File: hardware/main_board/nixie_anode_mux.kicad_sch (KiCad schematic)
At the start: 39 parts, among them Q10 MMBTA42, Q11 MMBTA92, Q12 MMBTA42, Q13 MMBTA92, Q14 MMBTA42, Q15 MMBTA92, Q4 MMBTA92, Q5 MMBTA42, Q6 MMBTA42, Q7 MMBTA92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

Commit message: chore(hardware): update bom and LCSC SN
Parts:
- C41: LCSC PN (none) -> C106248
- C42: LCSC PN (none) -> C36911391
- Q10, Q12, Q14, Q5, Q6, Q8: LCSC PN (none) -> C916394
- Q11, Q13, Q15, Q4, Q7, Q9: LCSC PN (none) -> C20069146
- R21, R39, R43, R47, R51, R55: LCSC PN (none) -> C105578
- R34, R38, R42, R46, R50, R54: LCSC PN (none) -> C114622
- R35, R40, R44, R48, R52, R56: LCSC PN (none) -> C105579
- R36, R37, R41, R45, R49, R53: LCSC PN (none) -> C98220
- U13: LCSC PN (none) -> C546729

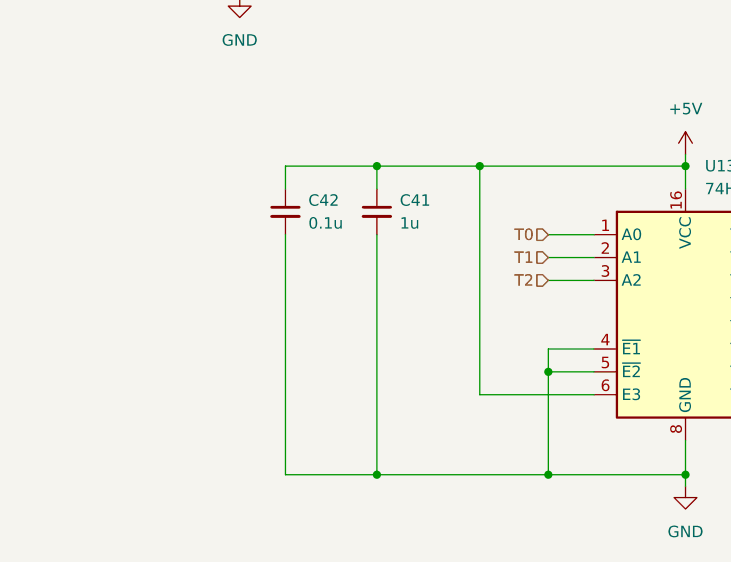
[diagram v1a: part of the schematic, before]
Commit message: hardware(schematic): update main control board schematic and layout
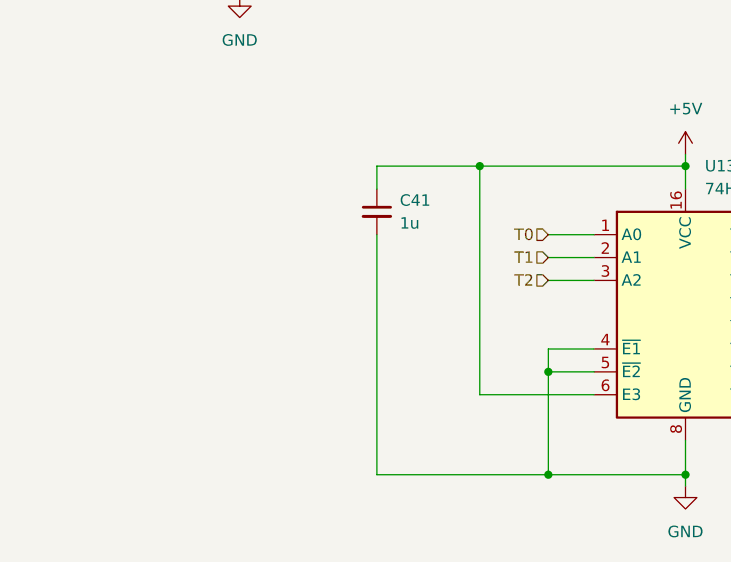
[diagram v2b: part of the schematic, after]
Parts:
- removed C42: 0.1u, Capacitor_SMD:C_0603_1608Metric, symbol Device:C_Small
- C41: LCSC PN C106248 -> C5199872
- Q10, Q12, Q14, Q5, Q6, Q8: LCSC PN C916394 -> C94389
- Q11, Q13, Q15, Q4, Q7, Q9: LCSC PN C20069146 -> C82049
- R21, R39, R43, R47, R51, R55: LCSC PN C105578 -> C22935
- R34, R38, R42, R46, R50, R54: LCSC PN C114622 -> C23178
- R35, R40, R44, R48, R52, R56: LCSC PN C105579 -> C25819
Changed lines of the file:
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@@
 	)
 	(junction
-		(at 55.88 176.53)
-		(diameter 0)
-		(color 0 0 0 0)
-	)
-	(junction
 		(at 125.73 49.53)
 		(diameter 0)
@@
 	)
 	(junction
-		(at 55.88 142.24)
-		(diameter 0)
-		(color 0 0 0 0)
-	)
-	(junction
 		(at 62.23 49.53)
 		(diameter 0)
@@
 	(wire
 		(pts
-			(xy 45.72 176.53) (xy 55.88 176.53)
-		)
-		(stroke
-			(width 0)
-			(type default)
-		)
-	)
-	(wire
-		(pts
 			(xy 190.5 30.48) (xy 190.5 36.83)
 		)
@@
 	(wire
 		(pts
-			(xy 45.72 144.78) (xy 45.72 142.24)
-		)
-		(stroke
-			(width 0)
-			(type default)
-		)
-	)
-	(wire
-		(pts
 			(xy 100.33 152.4) (xy 102.87 152.4)
 		)
@@
 	(wire
 		(pts
-			(xy 45.72 149.86) (xy 45.72 176.53)
-		)
-		(stroke
-			(width 0)
-			(type default)
-		)
-	)
-	(wire
-		(pts
 			(xy 30.48 113.03) (xy 33.02 113.03)
 		)
@@
 	(wire
 		(pts
-			(xy 45.72 142.24) (xy 55.88 142.24)
-		)
-		(stroke
-			(width 0)
-			(type default)
-		)
-	)
-	(wire
-		(pts
 			(xy 152.4 58.42) (xy 153.67 58.42)
 		)
@@
 			)
 		)
-		(property "LCSC PN" "C105578"
+		(property "LCSC PN" "C22935"
 			(at 180.34 45.72 0)
 			(effects
@@
 			)
 		)
-		(property "LCSC PN" "C114622"
+		(property "LCSC PN" "C23178"
 			(at 109.22 49.53 90)
 			(effects
@@
 			)
 		)
-		(property "LCSC PN" "C105579"
+		(property "LCSC PN" "C25819"
 			(at 201.93 106.68 90)
 			(effects
@@
 			)
 		)
-		(property "LCSC PN" "C106248"
+		(property "LCSC PN" "C5199872"
 			(at 55.88 147.32 0)
 			(effects
@@
 			)
 		)
-		(property "LCSC PN" "C105579"
+		(property "LCSC PN" "C25819"
 			(at 68.58 105.41 90)
 			(effects
@@
 			)
 		)
-		(property "LCSC PN" "C114622"
+		(property "LCSC PN" "C23178"
 			(at 45.72 105.41 90)
 			(effects
@@
 			)
 		)
-		(property "LCSC PN" "C916394"
+		(property "LCSC PN" "C94389"
 			(at 38.1 57.15 0)
 			(effects
@@
 			)
 		)
-		(property "LCSC PN" "C20069146"
+		(property "LCSC PN" "C82049"
 			(at 59.69 40.64 0)
 			(effects
@@
 			)
 		)
-		(property "LCSC PN" "C105579"
+		(property "LCSC PN" "C25819"
 			(at 196.85 50.8 90)
 			(effects
@@
 			)
 		)
-		(property "LCSC PN" "C105578"
+		(property "LCSC PN" "C22935"
 			(at 52.07 100.33 0)
 			(effects
@@
 			)
 		)
-		(property "LCSC PN" "C114622"
+		(property "LCSC PN" "C23178"
 			(at 110.49 105.41 90)
 			(effects
@@
 			)
 		)
-		(property "LCSC PN" "C20069146"
+		(property "LCSC PN" "C82049"
 			(at 59.69 96.52 0)
 			(effects
@@
 			)
 		)
-		(property "LCSC PN" "C105578"
+		(property "LCSC PN" "C22935"
 			(at 116.84 100.33 0)
 			(effects
@@
 			)
 		)
-		(property "LCSC PN" "C114622"
+		(property "LCSC PN" "C23178"
 			(at 45.72 49.53 90)
 			(effects
@@
 			)
 		)
-		(property "LCSC PN" "C105579"
+		(property "LCSC PN" "C25819"
 			(at 133.35 105.41 90)
 			(effects
@@
 			)
 		)
-		(property "LCSC PN" "C20069146"
+		(property "LCSC PN" "C82049"
 			(at 193.04 97.79 0)
 			(effects
@@
 			)
 		)
-		(property "LCSC PN" "C916394"
+		(property "LCSC PN" "C94389"
 			(at 171.45 114.3 0)
 			(effects
@@
 			)
 		)
-		(property "LCSC PN" "C114622"
+		(property "LCSC PN" "C23178"
 			(at 173.99 50.8 90)
 			(effects
@@
 			)
 		)
-		(property "LCSC PN" "C105578"
+		(property "LCSC PN" "C22935"
 			(at 185.42 101.6 0)
 			(effects
@@
 			)
 		)
-		(property "LCSC PN" "C20069146"
+		(property "LCSC PN" "C82049"
 			(at 187.96 41.91 0)
 			(effects
@@
 			)
 		)
-		(property "LCSC PN" "C916394"
+		(property "LCSC PN" "C94389"
 			(at 166.37 58.42 0)
 			(effects
@@
 			)
 		)
-		(property "LCSC PN" "C916394"
+		(property "LCSC PN" "C94389"
 			(at 38.1 113.03 0)
 			(effects
@@
 			)
 		)
-		(property "LCSC PN" "C916394"
+		(property "LCSC PN" "C94389"
 			(at 101.6 57.15 0)
 			(effects
@@
 			)
 		)
-		(property "LCSC PN" "C105579"
+		(property "LCSC PN" "C25819"
 			(at 132.08 49.53 90)
 			(effects
@@
 			)
 		)
-		(property "LCSC PN" "C105579"
+		(property "LCSC PN" "C25819"
 			(at 68.58 49.53 90)
 			(effects
@@
 			)
 		)
-		(property "LCSC PN" "C114622"
+		(property "LCSC PN" "C23178"
 			(at 179.07 106.68 90)
 			(effects
@@
 	)
 	(symbol
-		(lib_id "Device:C_Small")
-		(at 45.72 147.32 0)
-		(unit 1)
-		(exclude_from_sim no)
-		(in_bom yes)
-		(on_board yes)
-		(dnp no)
-		(fields_autoplaced yes)
-		(property "Reference" "C42"
-			(at 48.26 146.0562 0)
-			(effects
-				(font
-					(size 1.27 1.27)
-				)
-				(justify left)
-			)
-		)
-		(property "Value" "0.1u"
-			(at 48.26 148.5962 0)
-			(effects
-				(font
-					(size 1.27 1.27)
-				)
-				(justify left)
-			)
-		)
-		(property "Footprint" "Capacitor_SMD:C_0603_1608Metric"
-			(at 45.72 147.32 0)
-			(effects
-				(font
-					(size 1.27 1.27)
-				)
-				(hide yes)
-			)
-		)
-		(property "Datasheet" "~"
-			(at 45.72 147.32 0)
-			(effects
-				(font
-					(size 1.27 1.27)
-				)
-				(hide yes)
-			)
-		)
-		(property "Description" "Unpolarized capacitor, small symbol"
-			(at 45.72 147.32 0)
-			(effects
-				(font
-					(size 1.27 1.27)
-				)
-				(hide yes)
-			)
-		)
-		(property "LCSC PN" "C36911391"
-			(at 45.72 147.32 0)
-			(effects
-				(font
-					(size 1.27 1.27)
-				)
-				(hide yes)
-			)
-		)
-		(pin "1"
-		)
-		(pin "2"
-		)
-		(instances
-			(project "main_board"
-				(path "/62950e93-3f98-4dee-9256-8213caa98ee7/0cd333dd-e8ef-4279-9123-81fa88a25cdb"
-					(reference "C42")
-					(unit 1)
-				)
-			)
-		)
-	)
-	(symbol
 		(lib_id "Transistor_BJT:MMBTA92")
 		(at 123.19 40.64 0)
@@
 			)
 		)
-		(property "LCSC PN" "C20069146"
+		(property "LCSC PN" "C82049"
 			(at 123.19 40.64 0)
 			(effects
@@
 			)
 		)
-		(property "LCSC PN" "C20069146"
+		(property "LCSC PN" "C82049"
 			(at 124.46 96.52 0)
 			(effects
@@
 			)
 		)
-		(property "LCSC PN" "C916394"
+		(property "LCSC PN" "C94389"
 			(at 102.87 113.03 0)
 			(effects
@@
 			)
 		)
-		(property "LCSC PN" "C105578"
+		(property "LCSC PN" "C22935"
 			(at 52.07 44.45 0)
 			(effects
@@
 			)
 		)
-		(property "LCSC PN" "C105578"
+		(property "LCSC PN" "C22935"
 			(at 115.57 44.45 0)
 			(effects

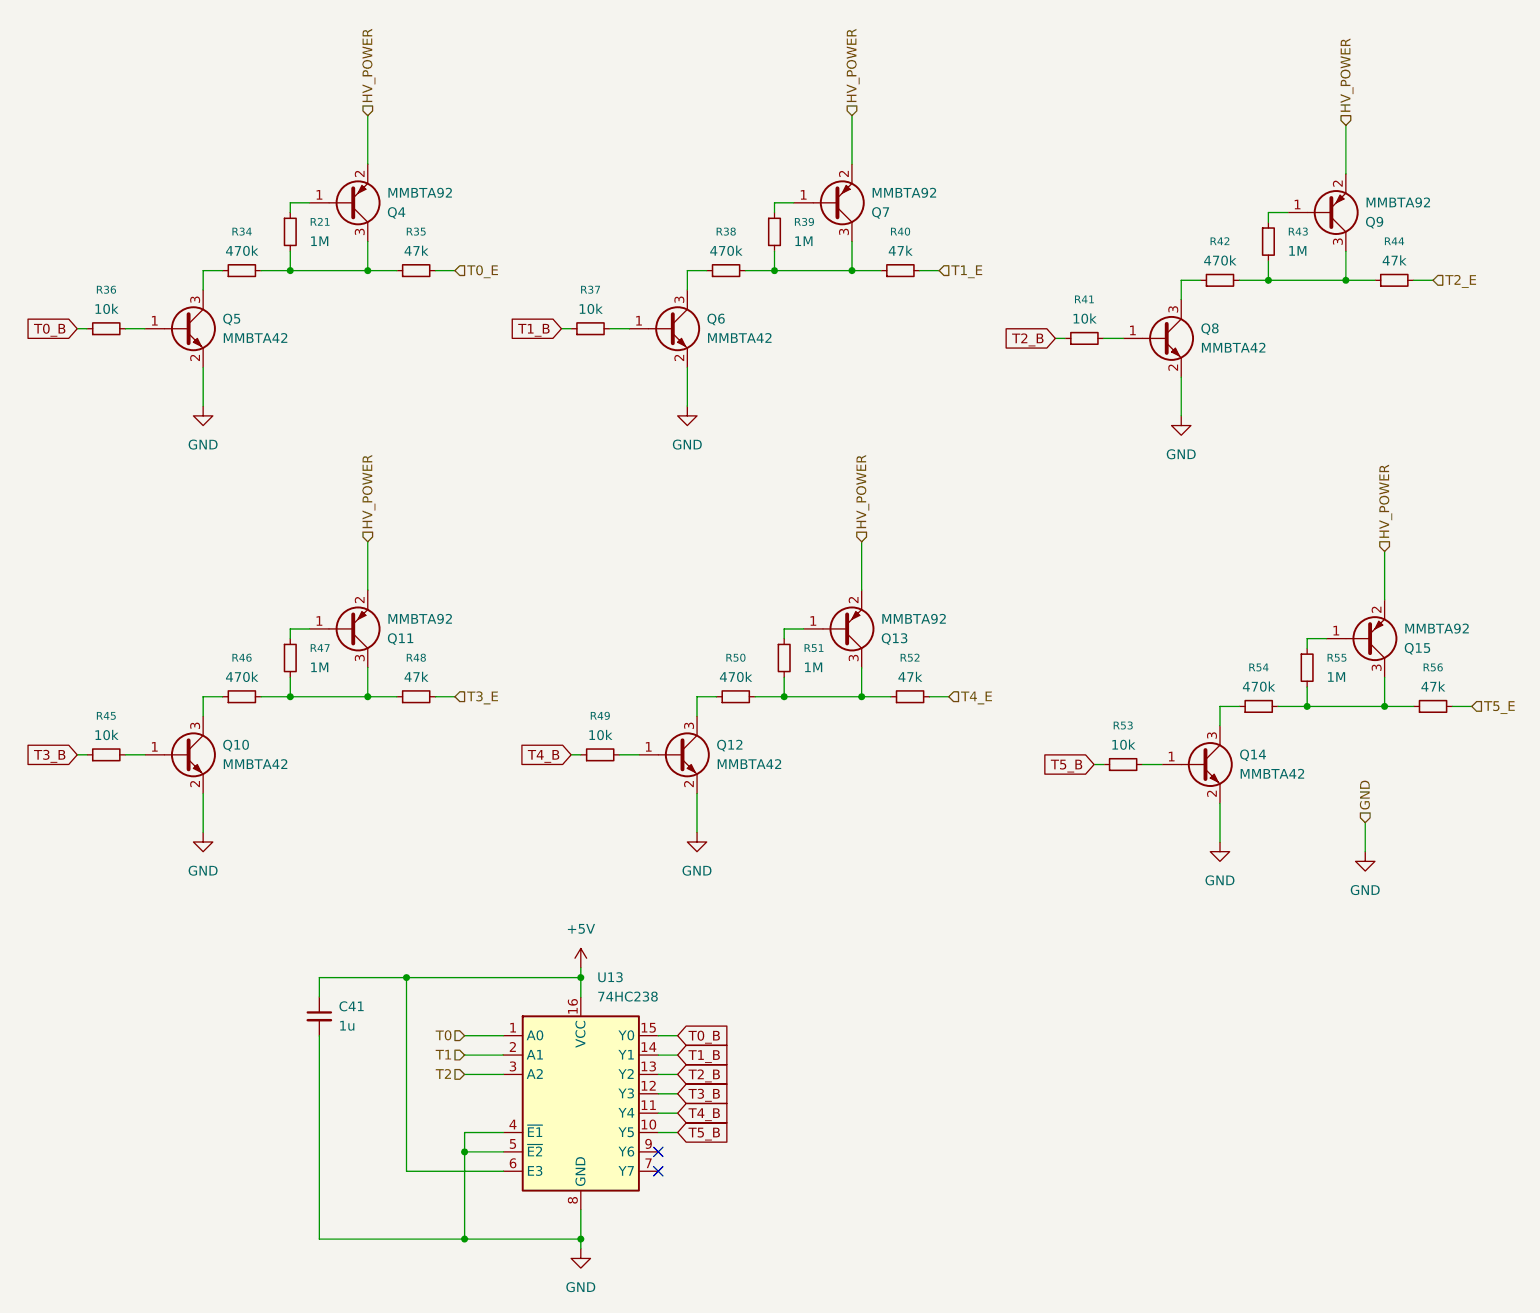
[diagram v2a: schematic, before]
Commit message: hardware(sch): update component package to 0402 as most as possable, layout is still need to complete
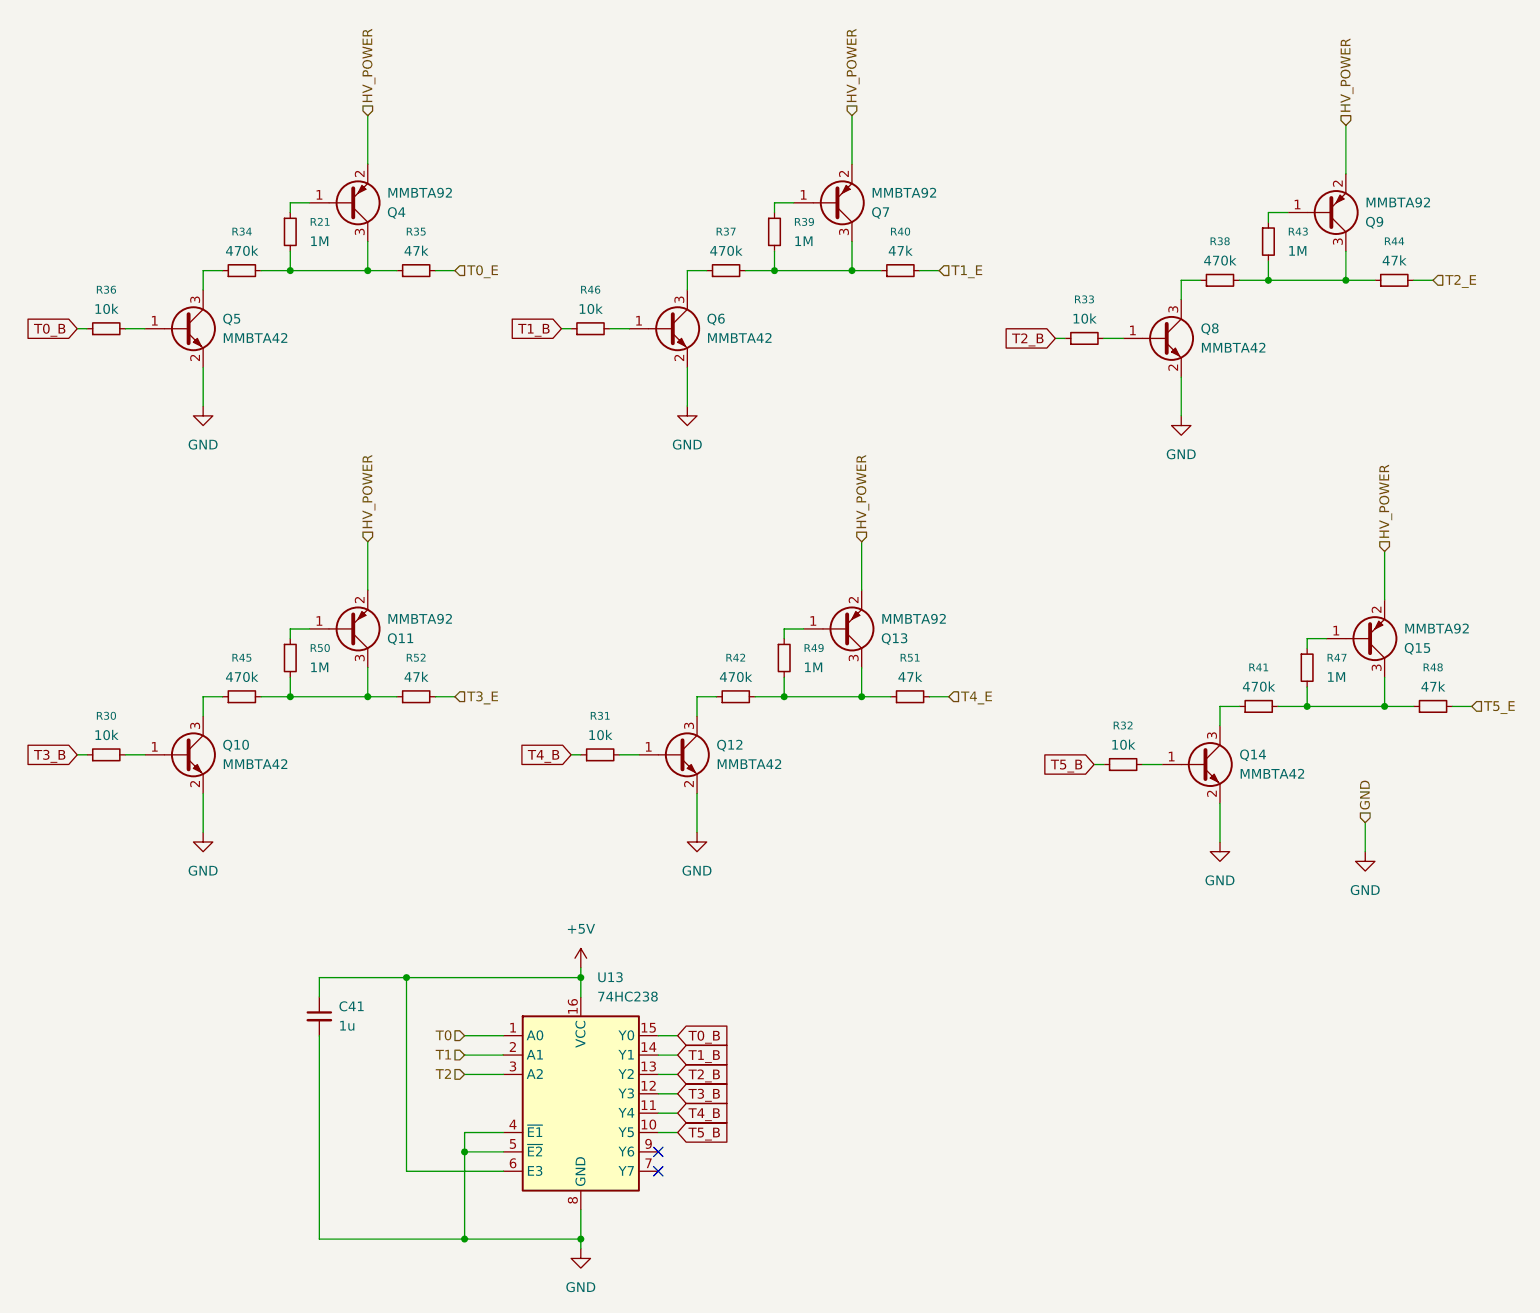
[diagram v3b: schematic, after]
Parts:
- removed R53: 10k, Resistor_SMD:R_0603_1608Metric, symbol Device:R_Small
- removed R54: 470k, Resistor_SMD:R_0603_1608Metric, symbol Device:R_Small
- removed R55: 1M, Resistor_SMD:R_0603_1608Metric, symbol Device:R_Small
- removed R56: 47k, Resistor_SMD:R_0603_1608Metric, symbol Device:R_Small
- added R30, R31, R32, R33: 10k, Resistor_SMD:R_0402_1005Metric, symbol Device:R_Small
- R21, R39, R43, R47: footprint Resistor_SMD:R_0603_1608Metric -> Resistor_SMD:R_0402_1005Metric; LCSC PN C22935 -> C26083
- R34, R38, R42: footprint Resistor_SMD:R_0603_1608Metric -> Resistor_SMD:R_0402_1005Metric; LCSC PN C23178 -> C25790
- R35, R40, R44, R48, R52: footprint Resistor_SMD:R_0603_1608Metric -> Resistor_SMD:R_0402_1005Metric; LCSC PN C25819 -> C25792
- R36: footprint Resistor_SMD:R_0603_1608Metric -> Resistor_SMD:R_0402_1005Metric; LCSC PN C98220 -> C25744
- R37, R41, R45: value 10k -> 470k; footprint Resistor_SMD:R_0603_1608Metric -> Resistor_SMD:R_0402_1005Metric; LCSC PN C98220 -> C25790
- R46: value 470k -> 10k; footprint Resistor_SMD:R_0603_1608Metric -> Resistor_SMD:R_0402_1005Metric; LCSC PN C23178 -> C25744
- R49: value 10k -> 1M; footprint Resistor_SMD:R_0603_1608Metric -> Resistor_SMD:R_0402_1005Metric; LCSC PN C98220 -> C26083
- R50: value 470k -> 1M; footprint Resistor_SMD:R_0603_1608Metric -> Resistor_SMD:R_0402_1005Metric; LCSC PN C23178 -> C26083
- R51: value 1M -> 47k; footprint Resistor_SMD:R_0603_1608Metric -> Resistor_SMD:R_0402_1005Metric; LCSC PN C22935 -> C25792
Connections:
- net T1_B: now also R46.1; no longer R37.1
- net T2_B: now also R33.1; no longer R41.1
- net T3_B: now also R30.1; no longer R45.1
- net T3_E: now also R52.2; no longer R48.2
- net T4_B: now also R31.1; no longer R49.1
- net T4_E: now also R51.2; no longer R52.2
- net T5_B: now also R32.1
- net T5_E: now also R48.2
- net at Q9.3 (C), R43.2, R44.1: now also R38.2; no longer R42.2
- net at R38.1: now also Q8.3 (C); no longer Q6.3 (C)
- net at Q7.3 (C), R39.2, R40.1: now also R37.2; no longer R38.2
- net at Q15.3 (C): now also R41.2, R47.2, R48.1
- net at Q10.1 (B): now also R30.2; no longer R45.2
- net at Q10.3 (C): now also R45.1; no longer R46.1
- net at Q14.1 (B): now also R32.2
- net at Q8.1 (B): now also R33.2; no longer R41.2
- net at Q12.1 (B): now also R31.2; no longer R49.2
- net at Q11.1 (B): now also R50.1; no longer R47.1
- net at Q12.3 (C): now also R42.1; no longer R50.1
- net at R50.2, R52.1: now also Q11.3 (C), R45.2; no longer Q13.3 (C), R51.2
- net at Q6.1 (B): now also R46.2; no longer R37.2
- net at R51.1: now also Q13.3 (C), R42.2, R49.2; no longer Q13.1 (B)
- net at Q15.1 (B): now also R47.1
- net at Q14.3 (C): now also R41.1
- new net: Q6.3 (C), R37.1
- new net: Q13.1 (B), R49.1
